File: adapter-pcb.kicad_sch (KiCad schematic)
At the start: 0 parts

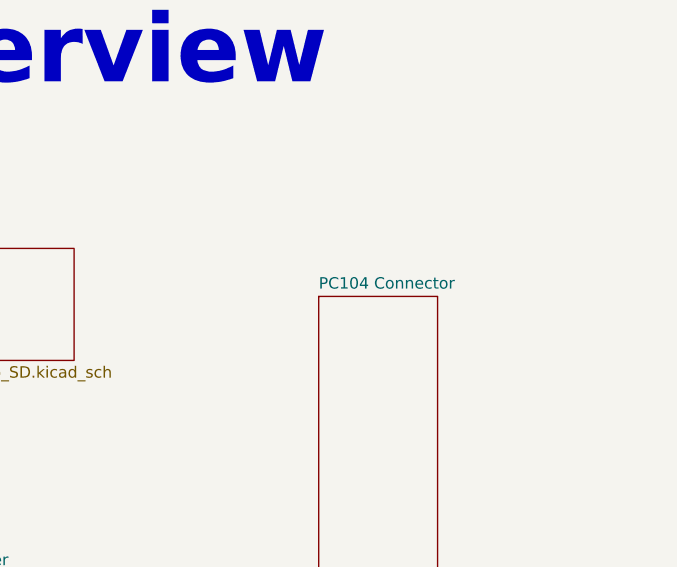
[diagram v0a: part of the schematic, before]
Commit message: Moved SD Card Slot
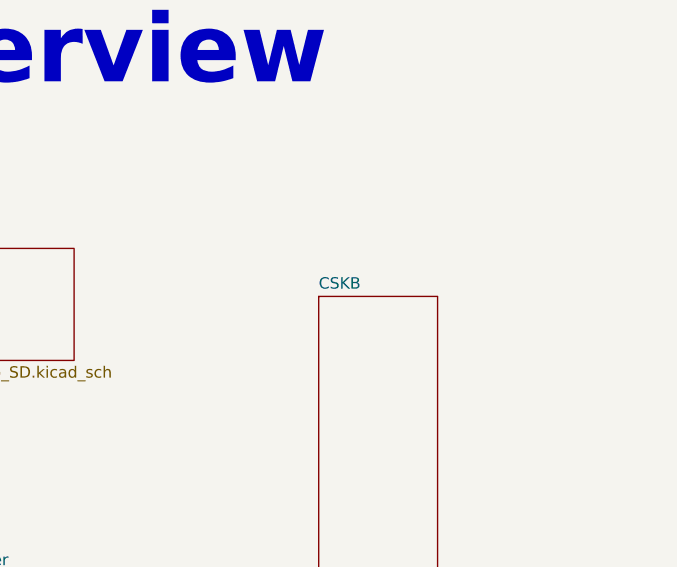
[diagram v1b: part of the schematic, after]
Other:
- sheet PC104 Connector renamed CSKB
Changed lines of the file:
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@@
 			(color 0 0 0 0.0000)
 		)
-		(property "Sheetname" "PC104 Connector"
+		(property "Sheetname" "CSKB"
 			(at 183.642 54.1524 0)
 			(effects

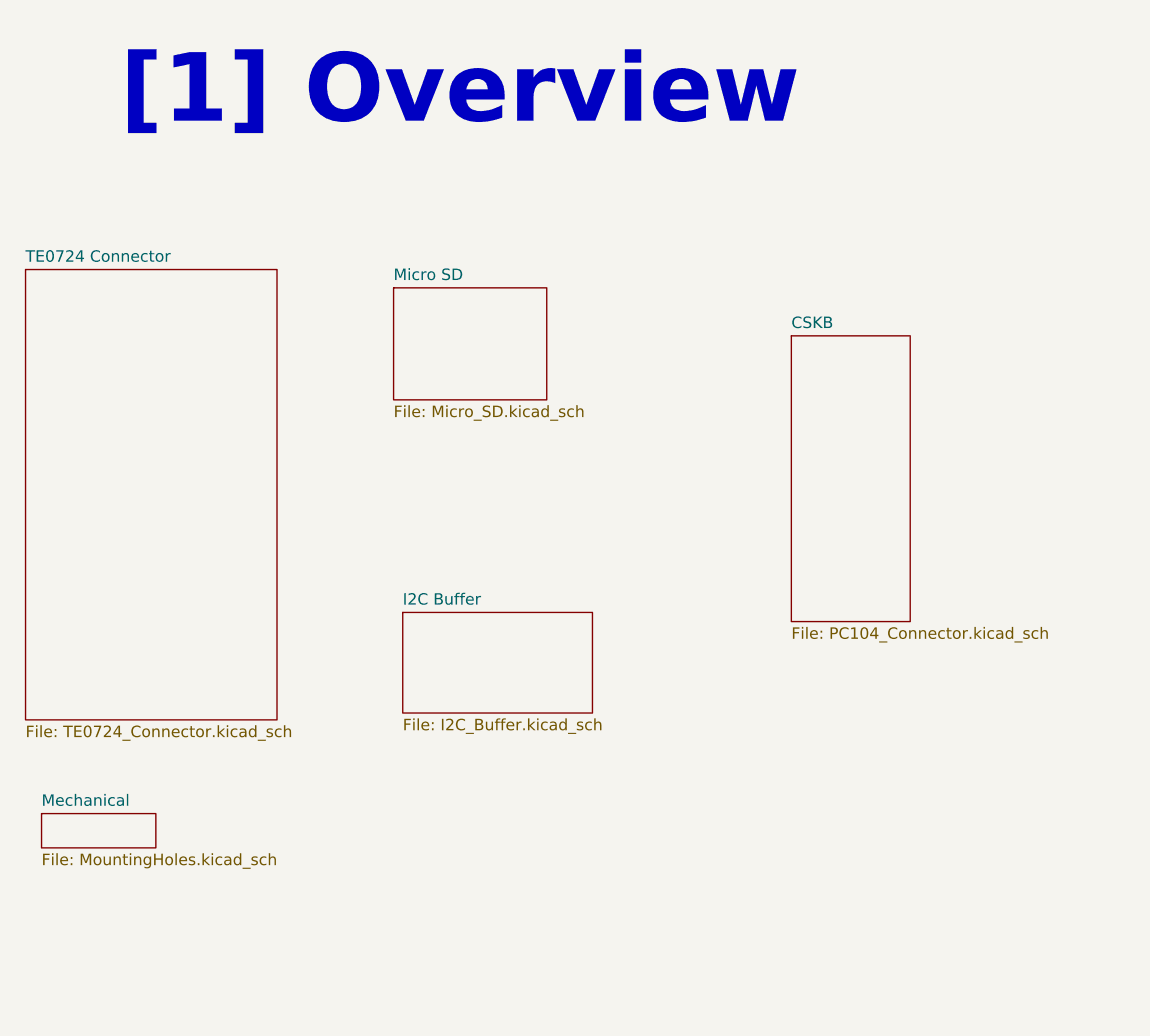
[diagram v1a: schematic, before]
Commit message: Added level shifter and breakout for ethernet
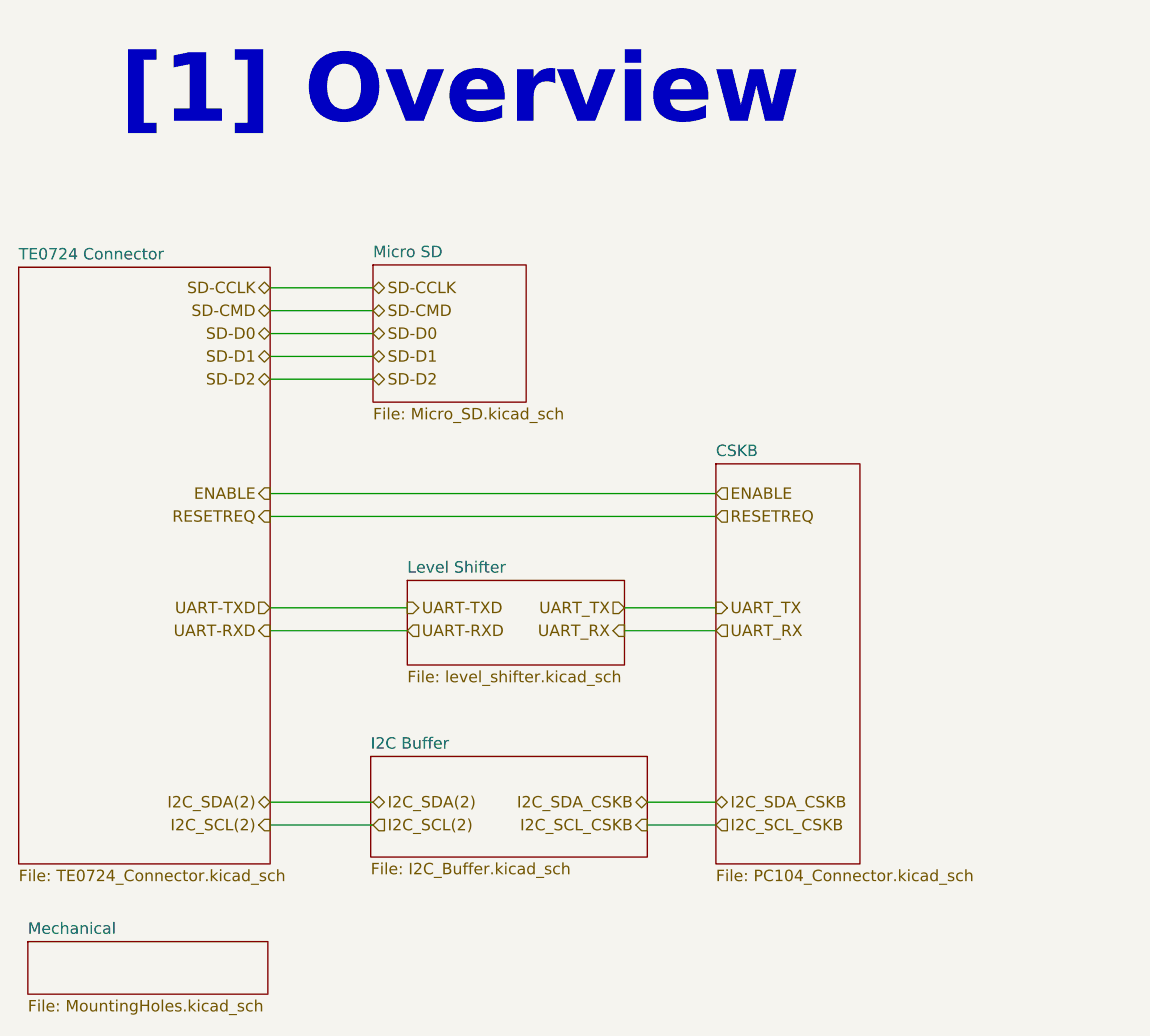
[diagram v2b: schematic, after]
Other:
- added sheet Level Shifter (level_shifter.kicad_sch)
